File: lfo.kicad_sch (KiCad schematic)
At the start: 7 parts, among them U4 Opamp_Dual

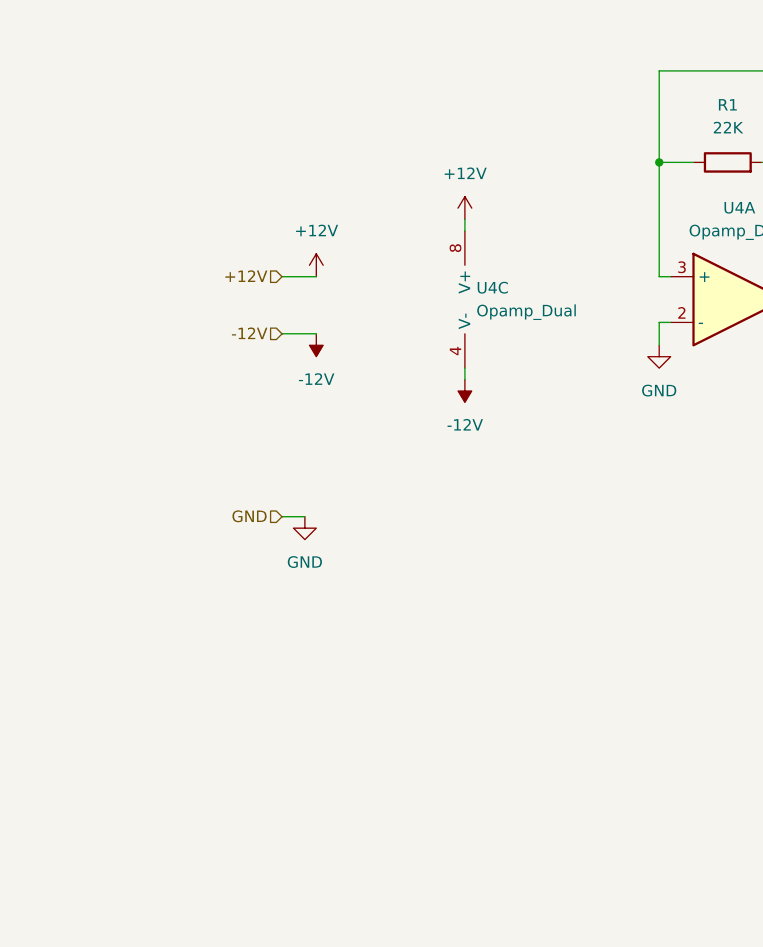
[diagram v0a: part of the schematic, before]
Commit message: Add missing values and connectors
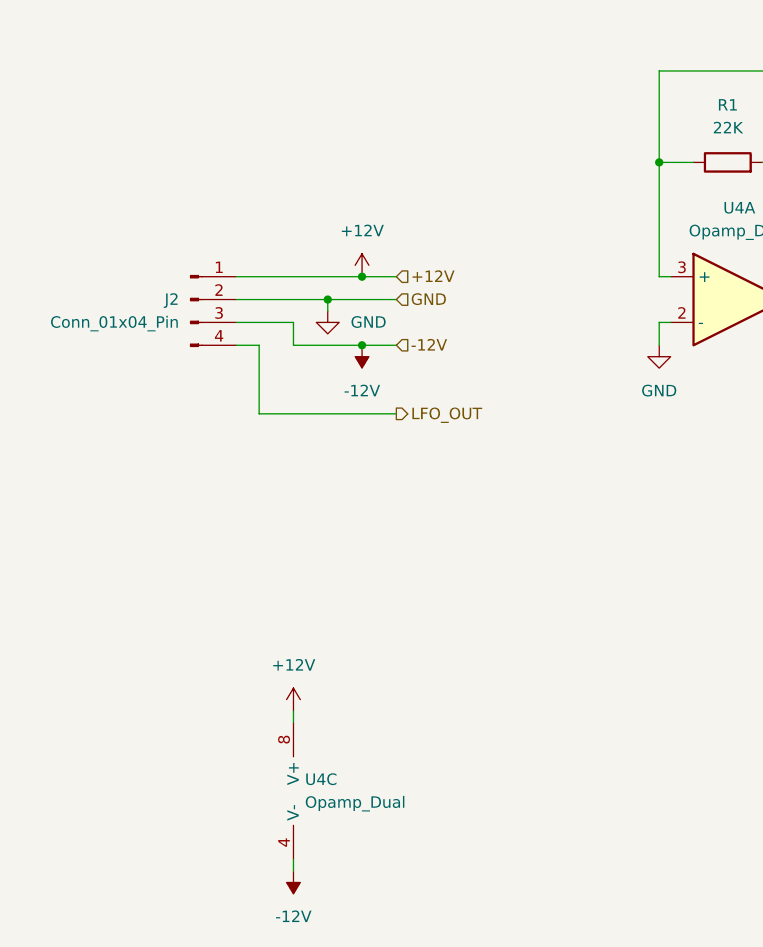
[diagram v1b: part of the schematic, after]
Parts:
- added J2: Conn_01x04_Pin, symbol Connector:Conn_01x04_Pin
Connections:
- net +12V: now also J2.1 (Pin_1)
- net -12V: now also J2.3 (Pin_3)
- net GND: now also J2.2 (Pin_2)
- net LFO_OUT: now also J2.4 (Pin_4)
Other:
- moved on the sheet: U4C

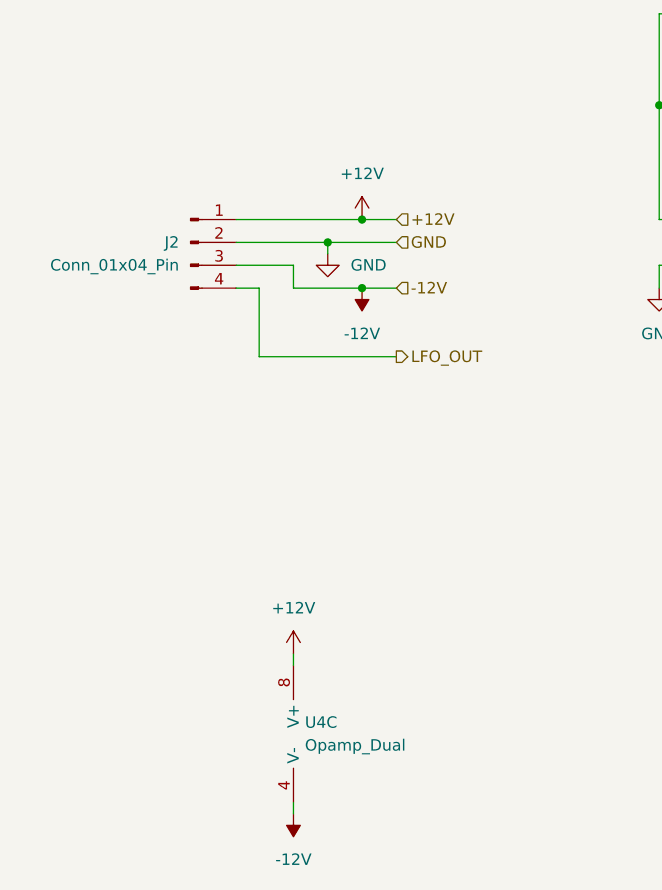
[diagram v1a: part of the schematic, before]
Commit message: Assign footprints and start PCB
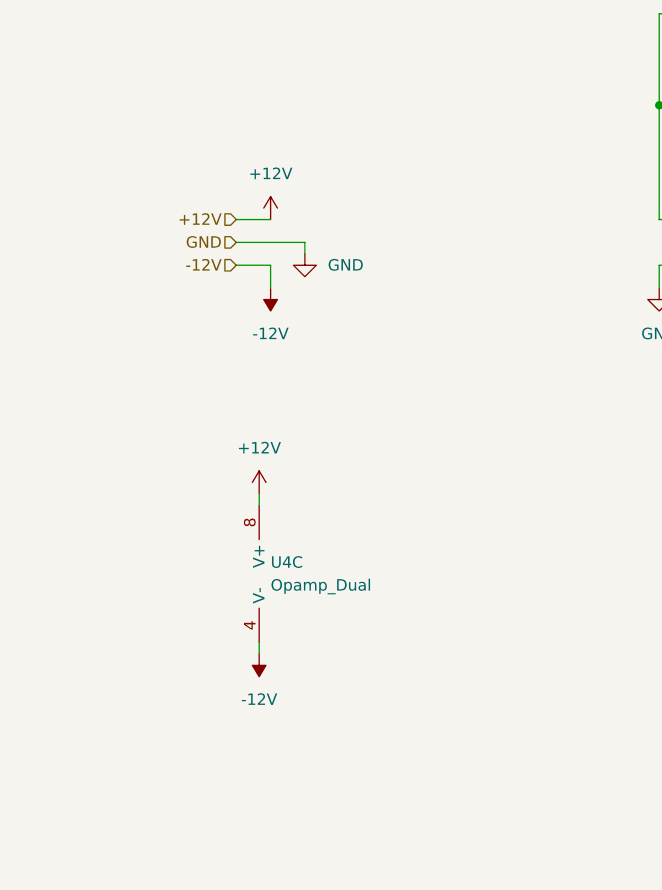
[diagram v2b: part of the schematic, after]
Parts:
- removed J2: Conn_01x04_Pin, symbol Connector:Conn_01x04_Pin
- C6: footprint (none) -> Capacitor_THT:C_Disc_D5.0mm_W2.5mm_P5.00mm
- R1, R2, R3, R4: footprint (none) -> Resistor_THT:R_Axial_DIN0204_L3.6mm_D1.6mm_P7.62mm_Horizontal
- RV1: footprint (none) -> Potentiometer_THT:Potentiometer_Omeg_PC16BU_Vertical
- U4: footprint (none) -> Package_DIP:DIP-8_W7.62mm_LongPads
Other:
- moved on the sheet: U4C

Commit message: VCO components are in position
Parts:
- C6: footprint Capacitor_THT:C_Disc_D5.0mm_W2.5mm_P5.00mm -> Capacitor_THT:C_Rect_L11.0mm_W2.8mm_P10.00mm_MKT
- R1, R2, R3, R4: footprint Resistor_THT:R_Axial_DIN0204_L3.6mm_D1.6mm_P7.62mm_Horizontal -> Resistor_THT:R_Axial_DIN0207_L6.3mm_D2.5mm_P15.24mm_Horizontal
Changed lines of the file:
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@@
 			)
 		)
-		(property "Footprint" "Capacitor_THT:C_Disc_D5.0mm_W2.5mm_P5.00mm"
+		(property "Footprint" "Capacitor_THT:C_Rect_L11.0mm_W2.8mm_P10.00mm_MKT"
 			(at 151.13 40.9448 0)
 			(effects
@@
 			)
 		)
-		(property "Footprint" "Resistor_THT:R_Axial_DIN0204_L3.6mm_D1.6mm_P7.62mm_Horizontal"
+		(property "Footprint" "Resistor_THT:R_Axial_DIN0207_L6.3mm_D2.5mm_P15.24mm_Horizontal"
 			(at 116.078 63.5 90)
 			(effects
@@
 			)
 		)
-		(property "Footprint" "Resistor_THT:R_Axial_DIN0204_L3.6mm_D1.6mm_P7.62mm_Horizontal"
+		(property "Footprint" "Resistor_THT:R_Axial_DIN0207_L6.3mm_D2.5mm_P15.24mm_Horizontal"
 			(at 106.68 58.928 90)
 			(effects
@@
 			)
 		)
-		(property "Footprint" "Resistor_THT:R_Axial_DIN0204_L3.6mm_D1.6mm_P7.62mm_Horizontal"
+		(property "Footprint" "Resistor_THT:R_Axial_DIN0207_L6.3mm_D2.5mm_P15.24mm_Horizontal"
 			(at 88.9 43.688 90)
 			(effects
@@
 			)
 		)
-		(property "Footprint" "Resistor_THT:R_Axial_DIN0204_L3.6mm_D1.6mm_P7.62mm_Horizontal"
+		(property "Footprint" "Resistor_THT:R_Axial_DIN0207_L6.3mm_D2.5mm_P15.24mm_Horizontal"
 			(at 106.68 29.972 90)
 			(effects

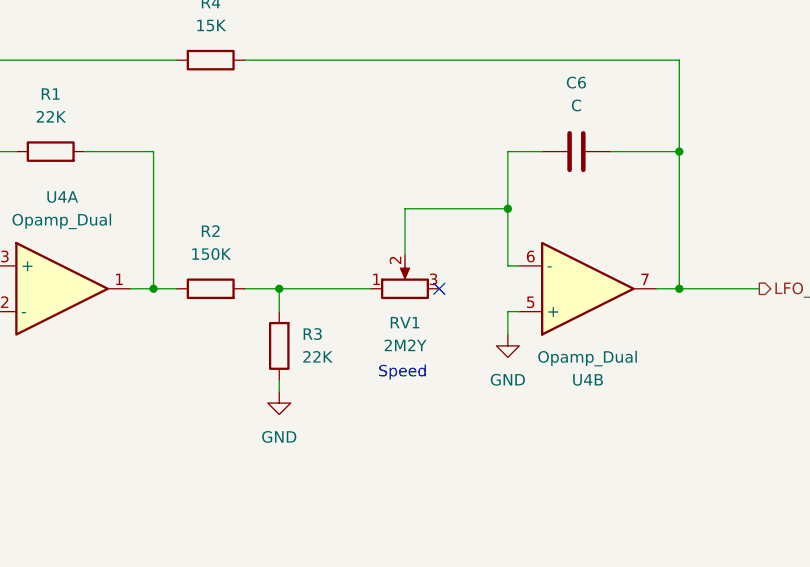
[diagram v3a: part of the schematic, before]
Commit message: Fix PCB sizes, adjust layout to new size
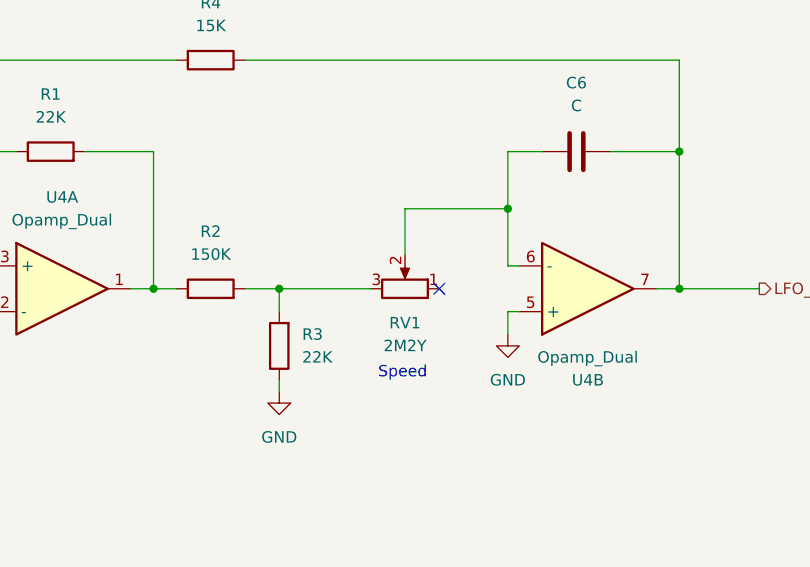
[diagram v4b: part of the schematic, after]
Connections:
- net at R2.2, R3.2: now also RV1.3; no longer RV1.1
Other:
- moved on the sheet: RV1
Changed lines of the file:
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@@
 	(symbol
 		(lib_id "Device:R_Potentiometer")
-		(at 128.27 57.15 90)
+		(at 128.27 57.15 270)
+		(mirror x)
 		(unit 1)
 		(exclude_from_sim no)
@@
 		(on_board yes)
 		(dnp no)
-		(fields_autoplaced yes)
 		(property "Reference" "RV1"
 			(at 128.27 60.96 90)

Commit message: Routing
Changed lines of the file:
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@@
+	(wire
+		(pts
+			(xy 167.64 60.96) (xy 158.75 60.96)
+		)
+		(stroke
+			(width 0)
+			(type default)
+		)
+	)
 	(wire
 		(pts
@@
 	(wire
 		(pts
+			(xy 158.75 60.96) (xy 158.75 57.15)
+		)
+		(stroke
+			(width 0)
+			(type default)
+		)
+	)
+	(wire
+		(pts
 			(xy 34.29 54.61) (xy 38.1 54.61)
 		)
@@
 			(width 0)
 			(type default)
+		)
+	)
+	(label "LFO_OUT"
+		(at 167.64 57.15 0)
+		(fields_autoplaced yes)
+		(effects
+			(font
+				(size 1.27 1.27)
+			)
+			(justify left bottom)
+		)
+		(property "Netclass" "LFO_OUT"
+			(at 167.64 58.42 0)
+			(effects
+				(font
+					(size 1.27 1.27)
+					(italic yes)
+				)
+				(justify left)
+			)
+		)
+	)
+	(hierarchical_label "LFO_OUT"
+		(shape output)
+		(at 167.64 60.96 0)
+		(effects
+			(font
+				(size 1.27 1.27)
+			)
+			(justify left)
 		)
 	)
@@
 		)
 	)
-	(hierarchical_label "LFO_OUT"
-		(shape output)
-		(at 167.64 57.15 0)
-		(effects
-			(font
-				(size 1.27 1.27)
-			)
-			(justify left)
-		)
-	)

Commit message: Routing
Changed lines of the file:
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@@
+		)
+	)
+	(label "GND"
+		(at 162.56 149.86 90)
+		(effects
+			(font
+				(size 1.27 1.27)
+			)
+			(justify left bottom)
 		)
 	)

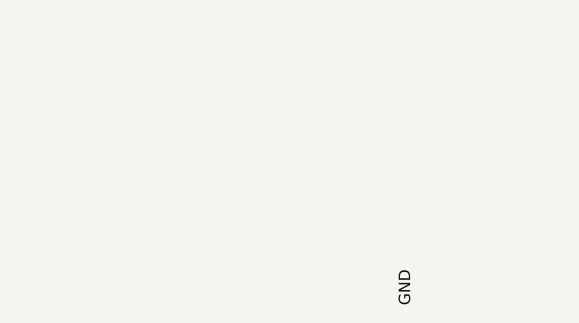
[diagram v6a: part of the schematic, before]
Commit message: Fixed VCF TRIG/GATE net, routed all except keyboard
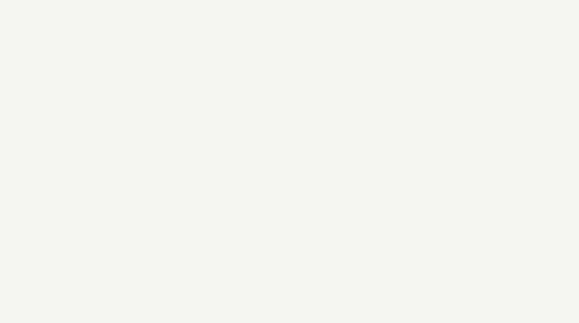
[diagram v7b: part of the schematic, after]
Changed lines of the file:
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@@
 		)
 	)
-	(label "GND"
-		(at 162.56 149.86 90)
+	(label "LFO_OUT"
+		(at 167.64 57.15 0)
 		(effects
 			(font
@@
 		)
 	)
-	(label "LFO_OUT"
-		(at 167.64 57.15 0)
-		(fields_autoplaced yes)
-		(effects
-			(font
-				(size 1.27 1.27)
-			)
-			(justify left bottom)
-		)
-		(property "Netclass" "LFO_OUT"
-			(at 167.64 58.42 0)
-			(effects
-				(font
-					(size 1.27 1.27)
-					(italic yes)
-				)
-				(justify left)
-			)
-		)
-	)

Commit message: Update README, add license to sheets
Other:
- title: (none) -> JEN SX-1000
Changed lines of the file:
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@@
 	(generator_version "9.0")
 	(paper "A4")
+	(title_block
+		(title "JEN SX-1000")
+		(comment 1 "SPDX-License-Identifier: CERN-OHL-S-2.0")
+	)
 	(text "Speed"
 		(exclude_from_sim no)
